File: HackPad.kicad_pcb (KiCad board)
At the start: 2 copper layers, 43.2 x 17.8 mm, 6 parts, among them J1 Analog, J2 Digital

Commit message: Finished the whole schematic. Started the PCB design.
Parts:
- added D1: D, Diode_THT:D_DO-35_SOD27_P7.62mm_Horizontal, F.Cu at (198.3, 140.0)
- added D10: D, Diode_THT:D_DO-35_SOD27_P7.62mm_Horizontal, F.Cu at (104.8, 121.0)
- added D11: D, Diode_THT:D_DO-35_SOD27_P7.62mm_Horizontal, F.Cu at (115.8, 81.0)
- added D12: D, Diode_THT:D_DO-35_SOD27_P7.62mm_Horizontal, F.Cu at (171.6, 159.1)
- added D13: D, Diode_THT:D_DO-35_SOD27_P7.62mm_Horizontal, F.Cu at (102.8, 139.5)
- added D14: D, Diode_THT:D_DO-35_SOD27_P7.62mm_Horizontal, F.Cu at (154.8, 82.5)
- added D15: D, Diode_THT:D_DO-35_SOD27_P7.62mm_Horizontal, F.Cu at (189.8, 159.0)
- added D16: D, Diode_THT:D_DO-35_SOD27_P7.62mm_Horizontal, F.Cu at (158.1, 131.0)
- added D2: D, Diode_THT:D_DO-35_SOD27_P7.62mm_Horizontal, F.Cu at (123.3, 140.5)
- added D3: D, Diode_THT:D_DO-35_SOD27_P7.62mm_Horizontal, F.Cu at (157.3, 144.0)
- added D4: D, Diode_THT:D_DO-35_SOD27_P7.62mm_Horizontal, F.Cu at (210.5, 159.4)
- added D5: D, Diode_THT:D_DO-35_SOD27_P7.62mm_Horizontal, F.Cu at (89.8, 159.5)
- added D6: D, Diode_THT:D_DO-35_SOD27_P7.62mm_Horizontal, F.Cu at (127.3, 159.0)
- added D7: D, Diode_THT:D_DO-35_SOD27_P7.62mm_Horizontal, F.Cu at (109.2, 159.0)
- added D8: D, Diode_THT:D_DO-35_SOD27_P7.62mm_Horizontal, F.Cu at (186.7, 120.4)
- added D9: D, Diode_THT:D_DO-35_SOD27_P7.62mm_Horizontal, F.Cu at (124.8, 121.0)
- added J1: Conn_01x04_Pin, Connector_PinHeader_2.54mm:PinHeader_1x04_P2.54mm_Vertical, F.Cu at (135.5, 104.2)
- added SW1: SW_Push, Button_Switch_Keyboard:SW_Cherry_MX_1.00u_PCB, F.Cu at (216.0, 162.4)
- added SW10: SW_Push, Button_Switch_Keyboard:SW_Cherry_MX_1.00u_PCB, F.Cu at (115.1, 162.4)
- added SW11: SW_Push, Button_Switch_Keyboard:SW_Cherry_MX_1.00u_PCB, F.Cu at (177.5, 162.4)
- added SW12: SW_Push, Button_Switch_Keyboard:SW_Cherry_MX_1.00u_PCB, F.Cu at (196.7, 162.4)
- added SW13: SW_Push, Button_Switch_Keyboard:SW_Cherry_MX_1.00u_PCB, F.Cu at (206.5, 143.4)
- added SW14: SW_Push, Button_Switch_Keyboard:SW_Cherry_MX_1.00u_PCB, F.Cu at (125.1, 143.4)
- added SW15: RotaryEncoder_Switch_MP, Rotary_Encoder:RotaryEncoder_Alps_EC11E-Switch_Vertical_H20mm, F.Cu at (146.6, 145.0)
- added SW2: SW_Push, Button_Switch_Keyboard:SW_Cherry_MX_1.00u_PCB, F.Cu at (131.1, 124.4)
- added SW3: SW_Push, Button_Switch_Keyboard:SW_Cherry_MX_1.00u_PCB, F.Cu at (112.0, 124.4)
- added SW4: SW_Push, Button_Switch_Keyboard:SW_Cherry_MX_1.00u_PCB, F.Cu at (106.1, 143.4)
- added SW5: SW_Push, Button_Switch_Keyboard:SW_Cherry_MX_1.00u_PCB, F.Cu at (96.1, 162.4)
- added SW6: SW_Push, Button_Switch_Keyboard:SW_Cherry_MX_1.00u_PCB, F.Cu at (182.0, 124.4)
- added SW7: SW_Push, Button_Switch_Keyboard:SW_Cherry_MX_1.00u_PCB, F.Cu at (187.5, 143.4)
- added SW8: SW_Push, Button_Switch_Keyboard:SW_Cherry_MX_1.00u_PCB, F.Cu at (260.0, 138.9)
- added SW9: SW_Push, Button_Switch_Keyboard:SW_Cherry_MX_1.00u_PCB, F.Cu at (134.2, 162.4)
- added U1: MOUDLE-SEEEDUINO-XIAO, RF_Module:MCU_Seeed_ESP32C3, F.Cu at (154.9, 102.9)
- added U2: COM-09032, COM-09032:XDCR_COM-09032, F.Cu at (153.8, 147.5)
- added U3: 74HC595, Package_DIP:DIP-16_W7.62mm, F.Cu at (164.0, 118.0)
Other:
- board outline removed
- board text removed: "ICSP"
- board text removed: "USB Mini-B"

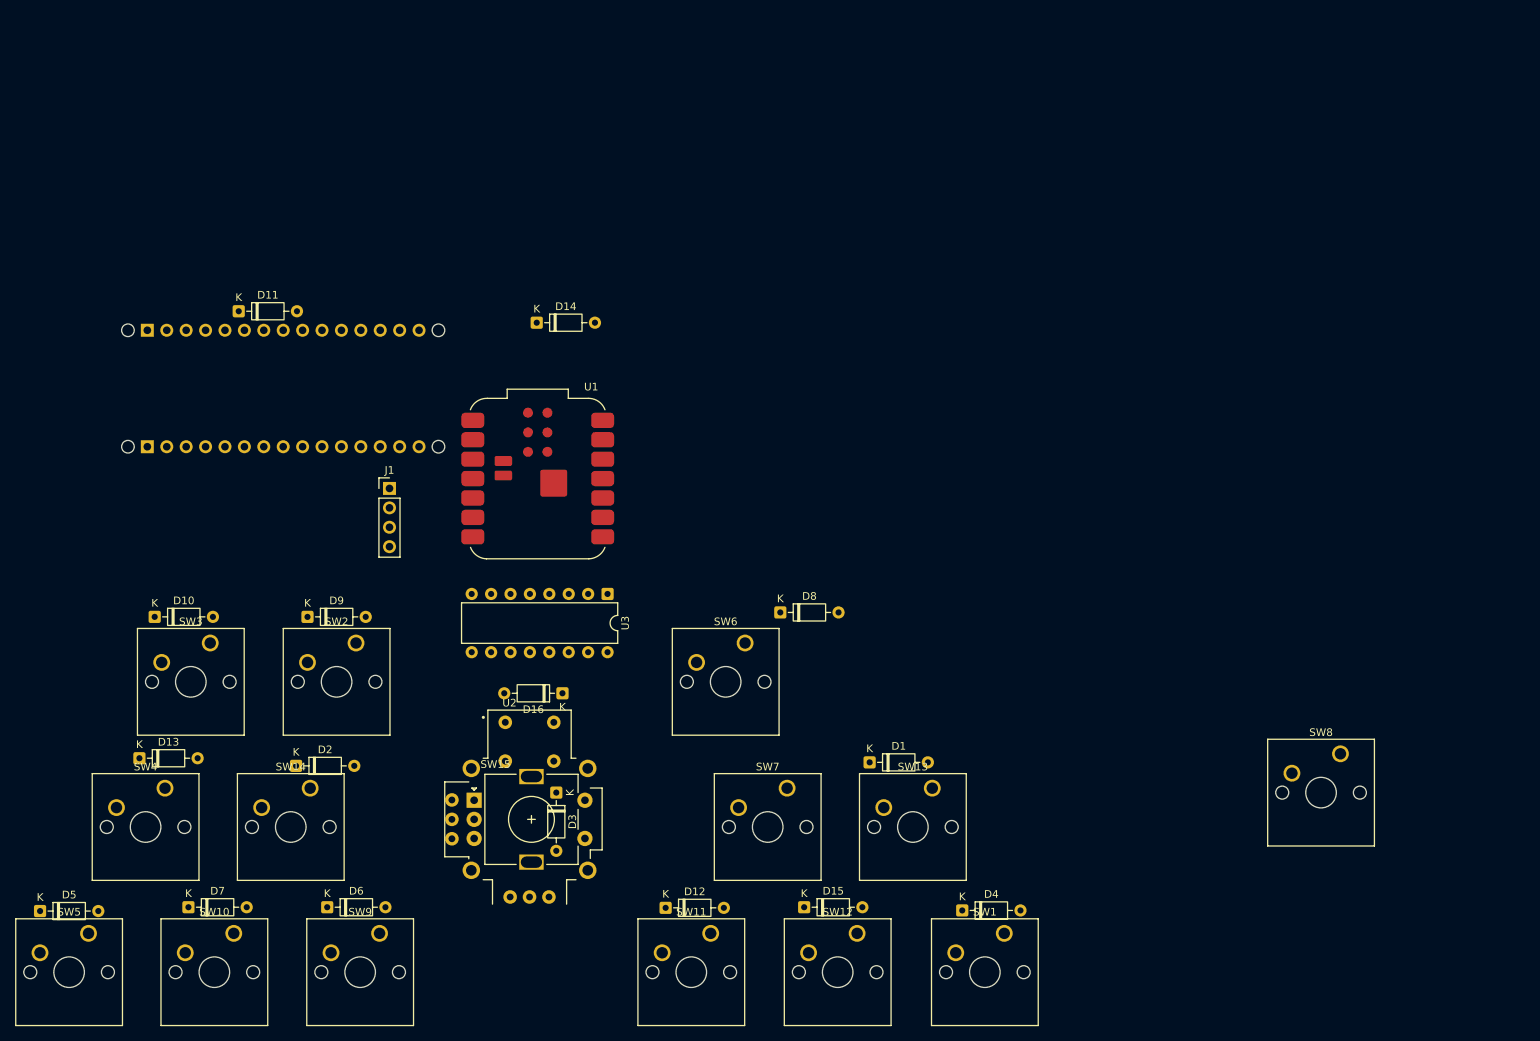
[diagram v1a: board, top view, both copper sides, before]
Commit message: Finished the whole schematic. Started the PCB layout
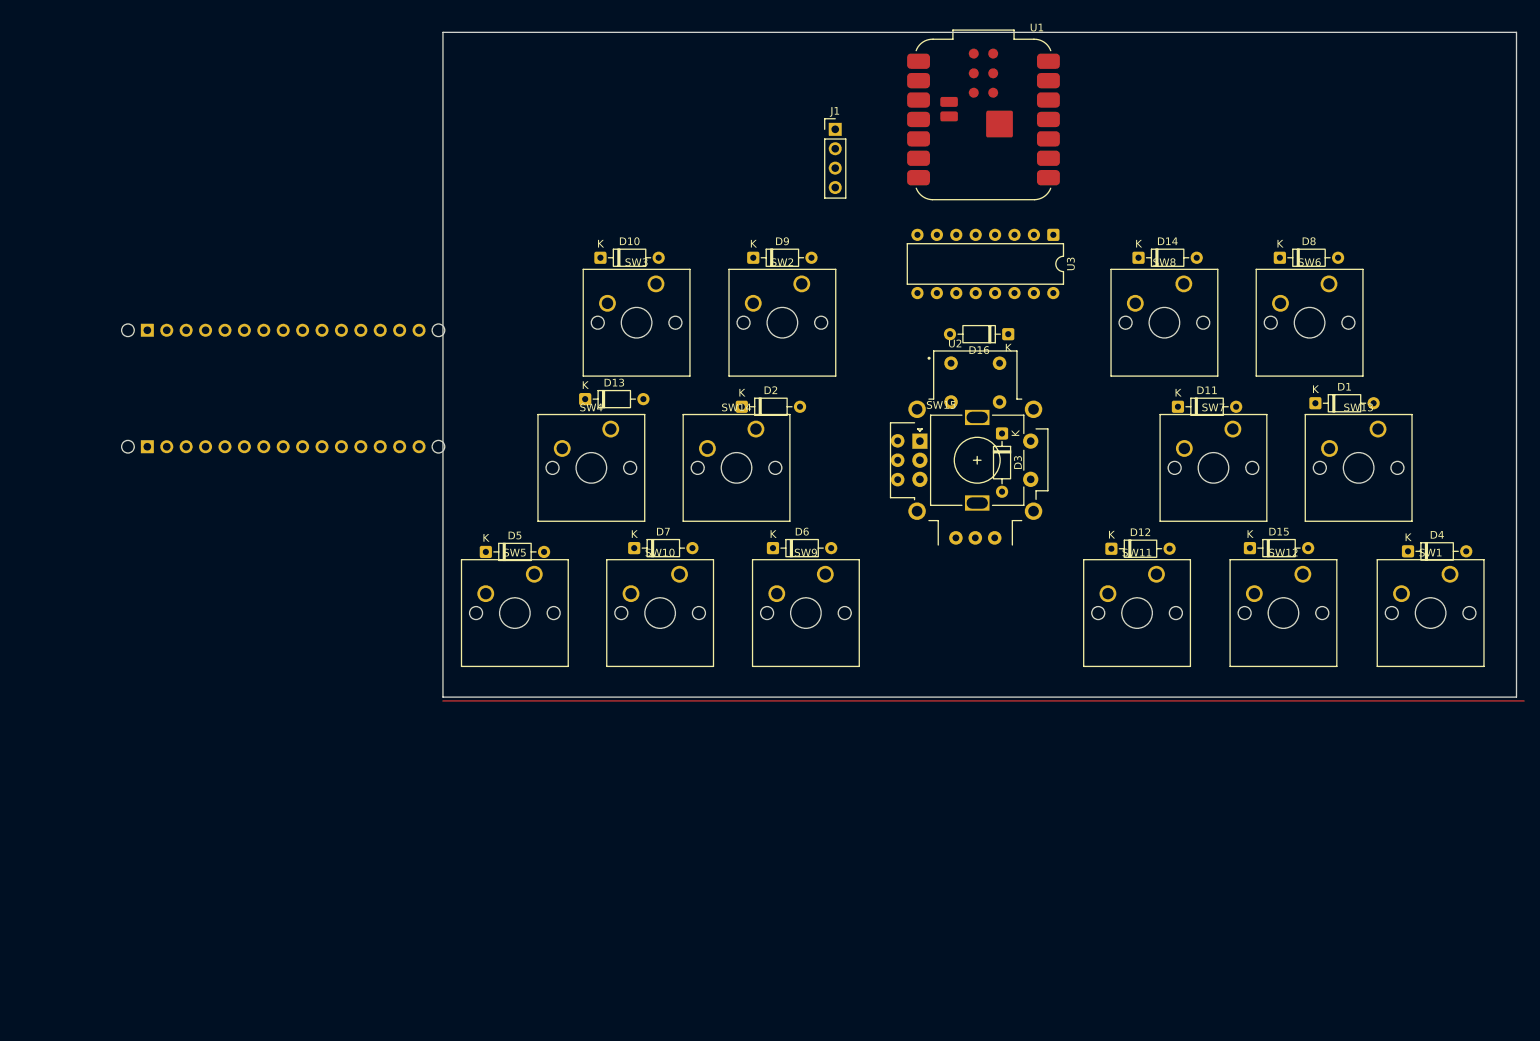
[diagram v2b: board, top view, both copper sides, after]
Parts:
- moved D11 123.6 mm to (238.7, 93.5)
- moved SW6 89.7 mm to (258.5, 77.4)
- moved D8 80.2 mm to (252.0, 74.0)
- moved D14 79.2 mm to (233.5, 74.0)
- moved D12 74.9 mm to (230.0, 112.1)
- moved D10 74.9 mm to (163.1, 74.0)
- moved D13 74.9 mm to (161.1, 92.5)
- moved D2 74.9 mm to (181.6, 93.5)
- moved D5 74.9 mm to (148.1, 112.5)
- moved D9 74.9 mm to (183.1, 74.0)
- moved U1 74.9 mm to (213.2, 55.9)
- moved D1 74.9 mm to (256.7, 93.0)
- moved D15 74.9 mm to (248.1, 112.0)
- moved D16 74.9 mm to (216.5, 84.0)
- moved D4 74.9 mm to (268.8, 112.4)
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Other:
- board outline added: 140.5 x 87 mm

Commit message: Finished the PCB completely
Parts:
- removed the J1 at (103.8, 98.7)
- removed J2: Digital, Connector_PinHeader_2.54mm:PinHeader_1x15_P2.54mm_Vertical
- removed MH1, MH2, MH3, MH4: MountingHole_65mil, Arduino_MountingHole:MountingHole_65mil
- added REF**: MountingHole_3.2mm, Arduino_MountingHole:MountingHole_3.2mm, F.Cu at (280.5, 112.5)
- added REF**: MountingHole_3.2mm, Arduino_MountingHole:MountingHole_3.2mm, F.Cu at (143.5, 129.0)
- added REF**: MountingHole_3.2mm, Arduino_MountingHole:MountingHole_3.2mm, F.Cu at (159.5, 68.5)
- added REF**: MountingHole_3.2mm, Arduino_MountingHole:MountingHole_3.2mm, F.Cu at (195.0, 47.5)
- added REF**: MountingHole_3.2mm, Arduino_MountingHole:MountingHole_3.2mm, F.Cu at (265.0, 72.0)
- added REF**: MountingHole_3.2mm, Arduino_MountingHole:MountingHole_3.2mm, F.Cu at (211.0, 128.5)
- moved U3 21.7 mm to (201.9, 78.1), turned to 90 degrees
- moved J1 5.67 mm to (198.0, 61.0), turned to 180 degrees
- moved D2 4.95 mm to (176.7, 93.0)
- moved D13 2.96 mm to (158.2, 93.0)
- moved D3 1.33 mm to (217.0, 97.0)
- moved D4 1.22 mm to (268.0, 111.5)
- moved D1 1.15 mm to (257.7, 92.5)
- moved D9 1.08 mm to (182.7, 73.0)
- moved D11 1.00 mm to (238.7, 92.5)
- moved D12 0.98 mm to (229.2, 111.5)
- moved D10 0.51 mm to (163.2, 73.5)
- moved D15 0.51 mm to (248.2, 111.5)
- moved D5 0.51 mm to (148.2, 112.0)
- moved D14 0.50 mm to (233.5, 73.5)
- moved D6 0.50 mm to (186.2, 112.0)
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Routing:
- net ROW3: track 0.00 -> 351.4 mm, vias 0 -> 1
- net ROW1: track 0.00 -> 239.9 mm, vias 0 -> 1
- net COL3: track 0.00 -> 203.1 mm, vias 0 -> 2
- net COL4: track 0.00 -> 183.9 mm, vias 0 -> 2
- net ROW4: track 0.00 -> 172.6 mm, vias 0 -> 2
- net COL1: track 0.00 -> 166.6 mm, vias 0 -> 7
- net ROW2: track 0.00 -> 162.6 mm, vias 0 -> 3
- net GND: track 0.16 -> 156.2 mm
- net COL2: track 0.00 -> 125.8 mm, vias 0 -> 2
- net VCC: track 0.00 -> 112.9 mm
- net Net-(J1-Pin_1): track 0.00 -> 70.9 mm, vias 0 -> 2
- net Net-(U1-PA11_A3_D3): track 0.00 -> 67.1 mm, vias 0 -> 1
- net Net-(U1-PA02_A0_D0): track 0.00 -> 66.7 mm
- net Net-(U1-PA4_A1_D1): track 0.00 -> 58.4 mm
- net Net-(U1-PA10_A2_D2): track 0.00 -> 49.8 mm, vias 0 -> 3
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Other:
- board size 140.5 x 87 mm -> 142 x 87 mm
